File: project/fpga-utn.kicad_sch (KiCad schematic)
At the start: 0 parts

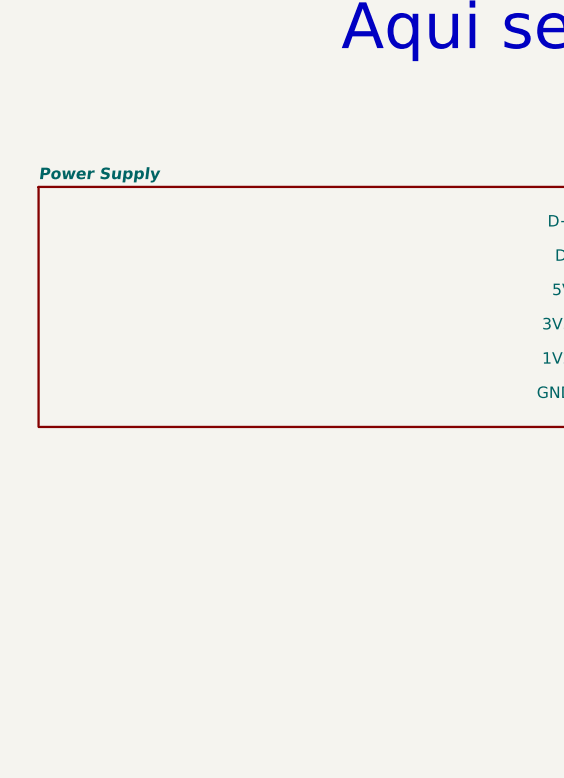
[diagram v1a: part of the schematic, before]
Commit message: DRC checkeado y fiduciales agregados
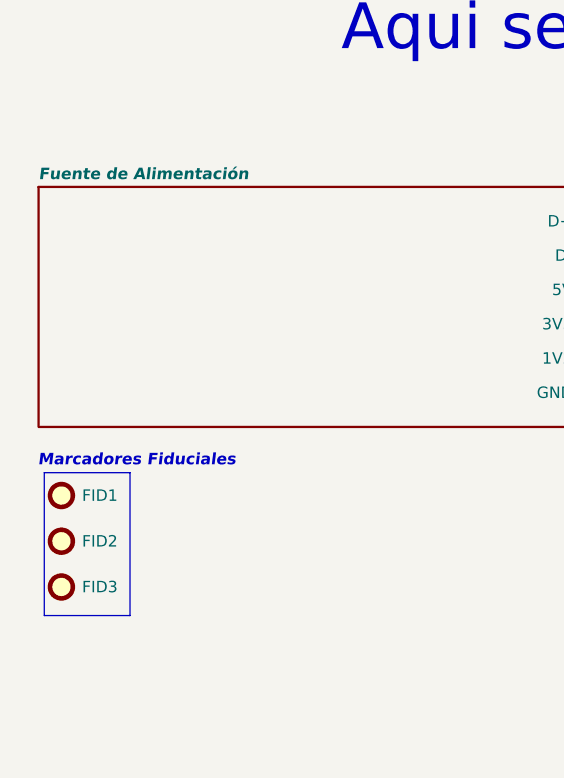
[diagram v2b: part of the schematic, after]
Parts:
- added FID1, FID2, FID3: Fiducial, Fiducial:Fiducial_1mm_Mask2mm, symbol Mechanical:Fiducial
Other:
- sheet Power Supply renamed Fuente de Alimentación
- note added: "Marcadores Fiduciales"
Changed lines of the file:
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@@
 	(generator_version "9.0")
 	(paper "A4")
+	(rectangle
+		(start 55.245 72.39)
+		(end 64.77 88.265)
+		(stroke
+			(width 0)
+			(type default)
+		)
+		(fill
+			(type none)
+		)
+	)
+	(text "Marcadores Fiduciales"
+		(exclude_from_sim no)
+		(at 65.532 71.12 0)
+		(effects
+			(font
+				(size 1.27 1.27)
+				(thickness 0.254)
+				(bold yes)
+				(italic yes)
+				(color 0 0 0 1)
+			)
+		)
+	)
 	(text "Aqui se inicia nuestro proyecto final"
 		(exclude_from_sim no)
@@
 			(width 0)
 			(type default)
+		)
+	)
+	(symbol
+		(lib_id "Mechanical:Fiducial")
+		(at 57.15 74.93 0)
+		(unit 1)
+		(exclude_from_sim no)
+		(in_bom yes)
+		(on_board yes)
+		(dnp no)
+		(property "Reference" "FID1"
+			(at 59.436 74.93 0)
+			(effects
+				(font
+					(size 1.27 1.27)
+				)
+				(justify left)
+			)
+		)
+		(property "Value" "Fiducial"
+			(at 59.69 76.1999 0)
+			(effects
+				(font
+					(size 1.27 1.27)
+				)
+				(justify left)
+				(hide yes)
+			)
+		)
+		(property "Footprint" "Fiducial:Fiducial_1mm_Mask2mm"
+			(at 57.15 74.93 0)
+			(effects
+				(font
+					(size 1.27 1.27)
+				)
+				(hide yes)
+			)
+		)
+		(property "Datasheet" "~"
+			(at 57.15 74.93 0)
+			(effects
+				(font
+					(size 1.27 1.27)
+				)
+				(hide yes)
+			)
+		)
+		(property "Description" "Fiducial Marker"
+			(at 57.15 74.93 0)
+			(effects
+				(font
+					(size 1.27 1.27)
+				)
+				(hide yes)
+			)
+		)
+		(instances
+			(project ""
+				(path "/fadb8841-cd7a-4174-937d-7c393e857c90"
+					(reference "FID1")
+					(unit 1)
+				)
+			)
+		)
+	)
+	(symbol
+		(lib_id "Mechanical:Fiducial")
+		(at 57.15 85.09 0)
+		(unit 1)
+		(exclude_from_sim no)
+		(in_bom yes)
+		(on_board yes)
+		(dnp no)
+		(property "Reference" "FID3"
+			(at 59.436 85.09 0)
+			(effects
+				(font
+					(size 1.27 1.27)
+				)
+				(justify left)
+			)
+		)
+		(property "Value" "Fiducial"
+			(at 59.69 86.3599 0)
+			(effects
+				(font
+					(size 1.27 1.27)
+				)
+				(justify left)
+				(hide yes)
+			)
+		)
+		(property "Footprint" "Fiducial:Fiducial_1mm_Mask2mm"
+			(at 57.15 85.09 0)
+			(effects
+				(font
+					(size 1.27 1.27)
+				)
+				(hide yes)
+			)
+		)
+		(property "Datasheet" "~"
+			(at 57.15 85.09 0)
+			(effects
+				(font
+					(size 1.27 1.27)
+				)
+				(hide yes)
+			)
+		)
+		(property "Description" "Fiducial Marker"
+			(at 57.15 85.09 0)
+			(effects
+				(font
+					(size 1.27 1.27)
+				)
+				(hide yes)
+			)
+		)
+		(instances
+			(project "fpga-utn"
+				(path "/fadb8841-cd7a-4174-937d-7c393e857c90"
+					(reference "FID3")
+					(unit 1)
+				)
+			)
+		)
+	)
+	(symbol
+		(lib_id "Mechanical:Fiducial")
+		(at 57.15 80.01 0)
+		(unit 1)
+		(exclude_from_sim no)
+		(in_bom yes)
+		(on_board yes)
+		(dnp no)
+		(property "Reference" "FID2"
+			(at 59.436 80.01 0)
+			(effects
+				(font
+					(size 1.27 1.27)
+				)
+				(justify left)
+			)
+		)
+		(property "Value" "Fiducial"
+			(at 59.69 81.2799 0)
+			(effects
+				(font
+					(size 1.27 1.27)
+				)
+				(justify left)
+				(hide yes)
+			)
+		)
+		(property "Footprint" "Fiducial:Fiducial_1mm_Mask2mm"
+			(at 57.15 80.01 0)
+			(effects
+				(font
+					(size 1.27 1.27)
+				)
+				(hide yes)
+			)
+		)
+		(property "Datasheet" "~"
+			(at 57.15 80.01 0)
+			(effects
+				(font
+					(size 1.27 1.27)
+				)
+				(hide yes)
+			)
+		)
+		(property "Description" "Fiducial Marker"
+			(at 57.15 80.01 0)
+			(effects
+				(font
+					(size 1.27 1.27)
+				)
+				(hide yes)
+			)
+		)
+		(instances
+			(project "fpga-utn"
+				(path "/fadb8841-cd7a-4174-937d-7c393e857c90"
+					(reference "FID2")
+					(unit 1)
+				)
+			)
 		)
 	)
@@
 			(color 0 0 0 0.0000)
 		)
-		(property "Sheetname" "Power Supply"
+		(property "Sheetname" "Fuente de Alimentación"
 			(at 54.61 39.9284 0)
 			(effects

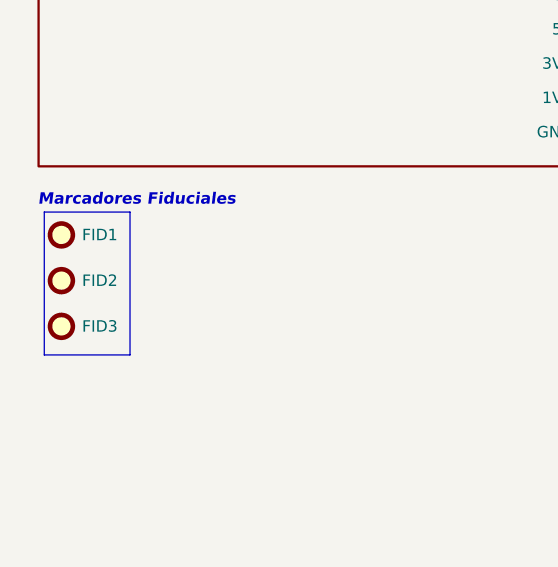
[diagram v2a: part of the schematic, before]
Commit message: Agregado de datasheets, cambio de regulador zener, ajuste de posicion de regulador, modelo 3d de oscilador
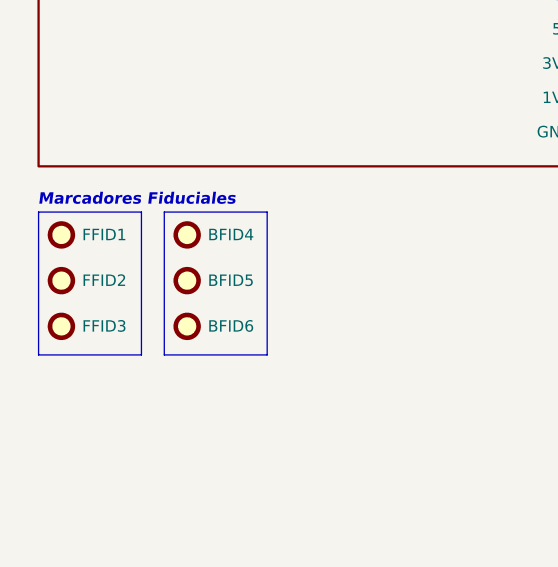
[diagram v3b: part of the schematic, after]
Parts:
- added BFID4, BFID5, BFID6: Fiducial, Fiducial:Fiducial_1mm_Mask2mm, symbol Mechanical:Fiducial
- renumbered FID1 to FFID1, FID2 to FFID2, FID3 to FFID3

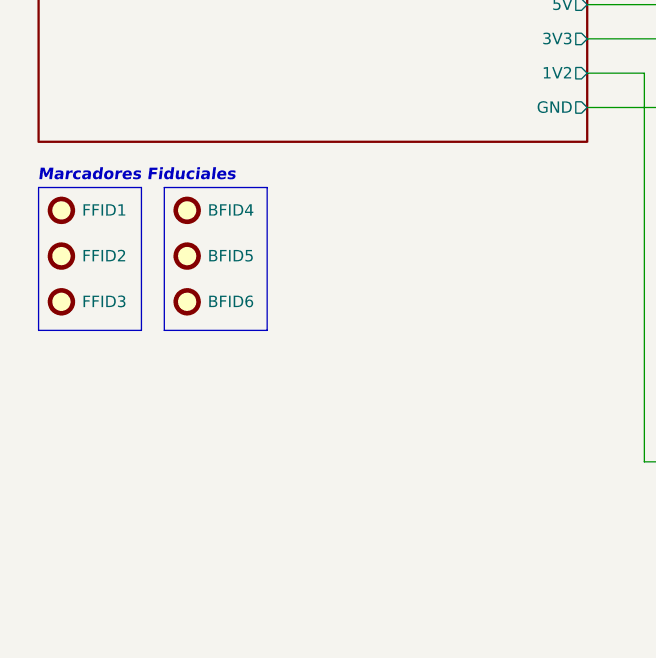
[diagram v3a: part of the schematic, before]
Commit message: Pistas, pads, soldermask y silkscreen corregidas para pasar analisis DMF de jlcpcb.
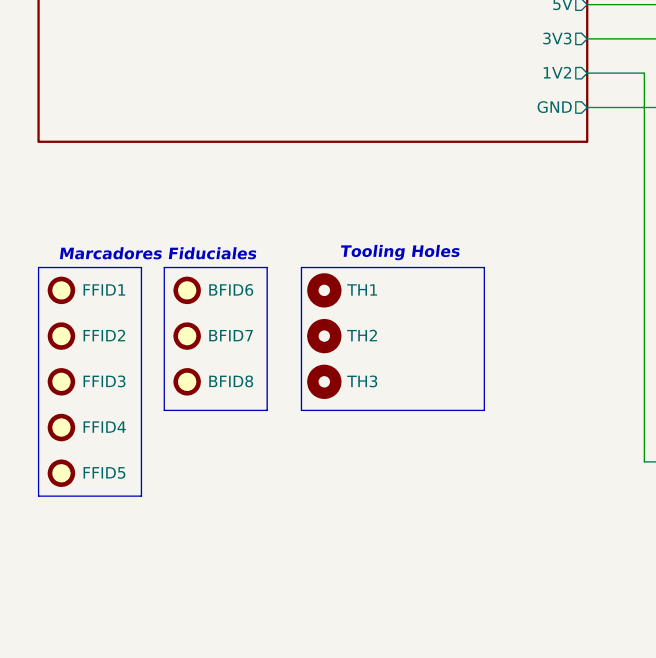
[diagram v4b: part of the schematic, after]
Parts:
- added FFID4, FFID5: Fiducial, Fiducial:Fiducial_1mm_Mask2mm, symbol Mechanical:Fiducial
- added TH1, TH2, TH3: MountingHole, MountingHole:ToolingHole_1.152mm, symbol Mechanical:MountingHole
- renumbered BFID4 to BFID6, BFID5 to BFID7, BFID6 to BFID8
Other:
- note added: "Tooling Holes"
- moved on the sheet: BFID6, BFID7, BFID8, FFID1, FFID2, FFID3

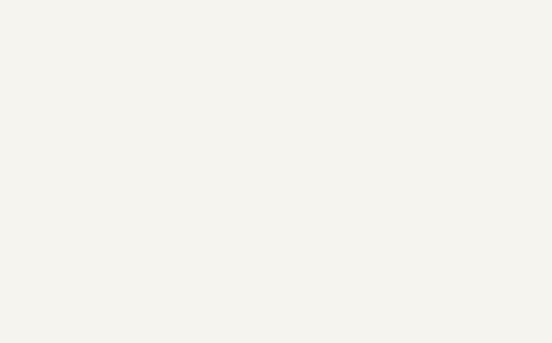
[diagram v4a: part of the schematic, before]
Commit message: Agregada licencia CERN-OHL-P-2.0
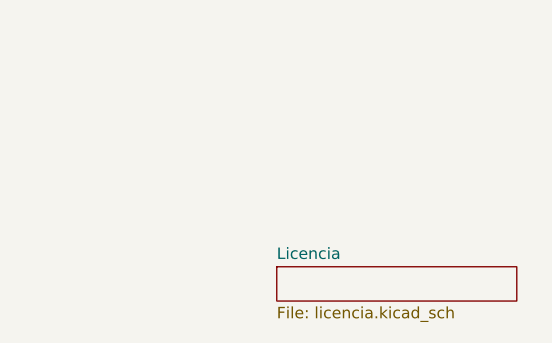
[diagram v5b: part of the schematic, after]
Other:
- added sheet Licencia (licencia.kicad_sch)
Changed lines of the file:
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@@
+	)
+	(sheet
+		(at 255.27 173.99)
+		(size 26.67 3.81)
+		(exclude_from_sim no)
+		(in_bom yes)
+		(on_board yes)
+		(dnp no)
+		(fields_autoplaced yes)
+		(stroke
+			(width 0.1524)
+			(type solid)
+		)
+		(fill
+			(color 0 0 0 0.0000)
+		)
+		(property "Sheetname" "Licencia"
+			(at 255.27 173.2784 0)
+			(effects
+				(font
+					(size 1.27 1.27)
+				)
+				(justify left bottom)
+			)
+		)
+		(property "Sheetfile" "licencia.kicad_sch"
+			(at 255.27 178.3846 0)
+			(effects
+				(font
+					(size 1.27 1.27)
+				)
+				(justify left top)
+			)
+		)
+		(instances
+			(project "fpga-utn"
+				(path "/fadb8841-cd7a-4174-937d-7c393e857c90"
+					(page "6")
+				)
+			)
+		)
 	)
 	(sheet
